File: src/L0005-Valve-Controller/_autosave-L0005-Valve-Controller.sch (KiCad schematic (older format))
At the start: 50 parts, among them J1 Jumper_NO, J2 Jumper_NO, P1 3220-20-0200-00, P10 353620650, P11 353620650, P12 353620650, P13 353620650, P14 647676-3, P15 647676-3, P2 140-504-415-000, P9 647676-2, U1 LPC54113J256BD64QL, U2 LMS8117AMP-3.3_NOPB, U3 MAX3370EXK+T, U4 MAX3370EXK+T

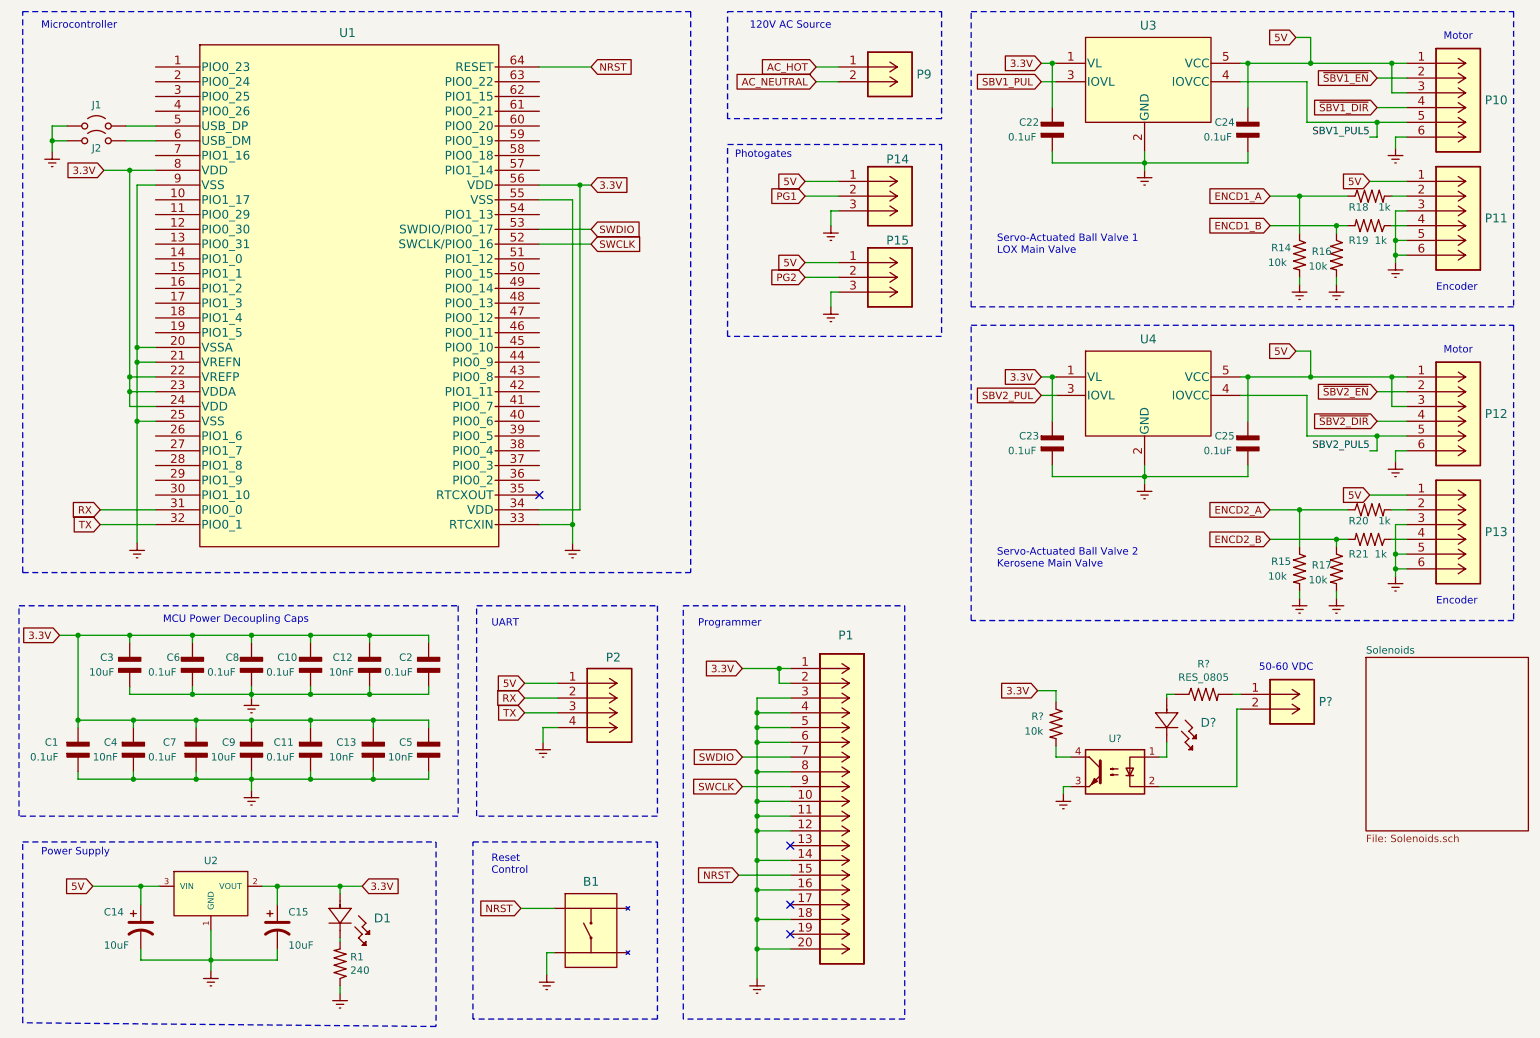
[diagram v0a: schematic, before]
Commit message: Added Red LED to lib files
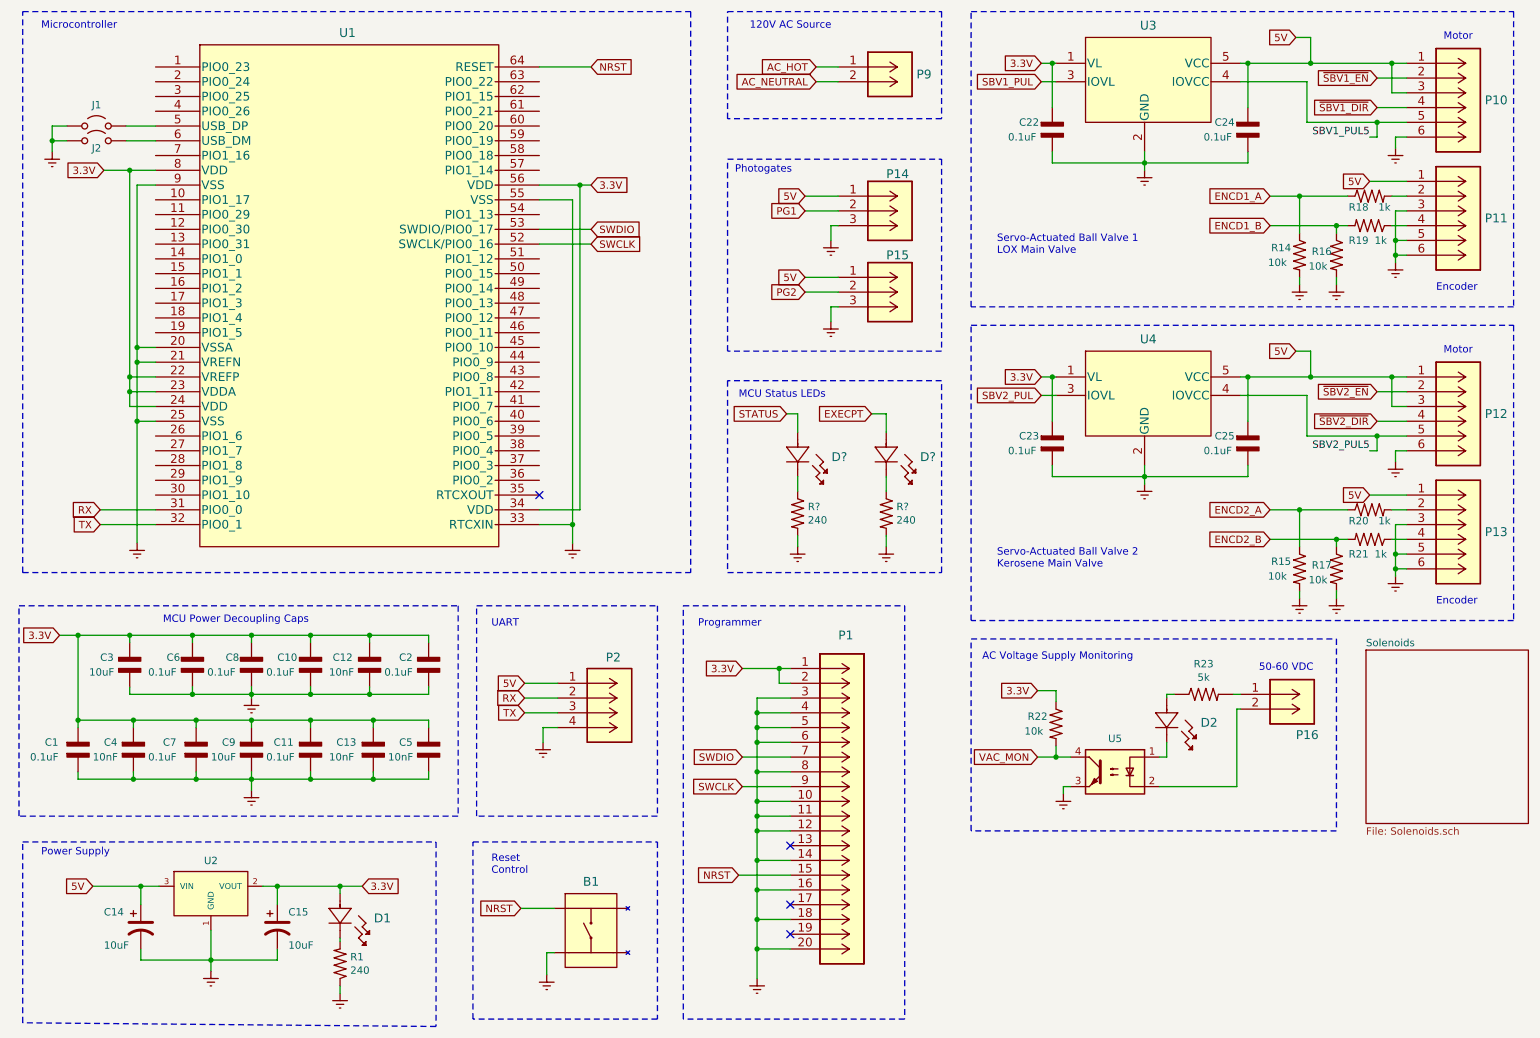
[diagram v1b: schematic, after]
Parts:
- added D?: LED_AMBER, symbol L0005-Valve-Controller:LED_AMBER
- added D?: LED_RED, symbol L0005-Valve-Controller:LED_RED
- added R? (x2): 240, symbol L0005-Valve-Controller:RES_0603
- R23: renamed from R?; value RES_0805 -> 5k
- gave numbers to parts that had none: 4
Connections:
- net Earth: now also R?.2, R?.2
- net VAC_MON: now reaches R22.2, U5.4
- new net: D?.1, R?.1 (x2)
- new net EXECPT: D?.2
- new net STATUS: D?.2
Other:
- note added: "AC Voltage Supply Monitoring"
- note added: "MCU Status LEDs"
- moved on the sheet: P14, P15
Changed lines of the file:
@@
 Microcontroller
 $Sheet
-S 9900 5125 1100 1175
+S 9900 5075 1100 1175
 U 624AA92C
 F0 "Solenoids" 50
@@
 L L0005-Valve-Controller:647676-3 P14
 U 1 1 62BF4641
-P 6325 1900
-F 0 "P14" H 6650 2050 60  0000 L CNN
-F 1 "647676-3" H 6675 1450 60  0001 C CNN
-F 2 "CONN_2043-1X04G00DAU_OUP" H 6675 1350 60  0001 C CNN
-F 3 "" H 6325 1900 60  0001 C CNN
-	1    6325 1900
-	1    0    0    -1
-$EndComp
-Text GLabel 6100 1900 0    50   Input ~ 0
+P 6325 2000
+F 0 "P14" H 6650 2150 60  0000 L CNN
+F 1 "647676-3" H 6675 1550 60  0001 C CNN
+F 2 "CONN_2043-1X04G00DAU_OUP" H 6675 1450 60  0001 C CNN
+F 3 "" H 6325 2000 60  0001 C CNN
+	1    6325 2000
+	1    0    0    -1
+$EndComp
+Text GLabel 6100 2000 0    50   Input ~ 0
 5V
 Wire Wire Line
-	6100 1900 6325 1900
+	6100 2000 6325 2000
 $Comp
 L L0005-Valve-Controller:Earth #PWR027
 U 1 1 62C26EB7
-P 6275 2200
-F 0 "#PWR027" H 6275 1950 50  0001 C CNN
-F 1 "Earth" H 6275 2050 50  0001 C CNN
-F 2 "" H 6275 2200 50  0001 C CNN
-F 3 "" H 6275 2200 50  0001 C CNN
-	1    6275 2200
-	1    0    0    -1
-$EndComp
-Wire Wire Line
-	6275 2200 6275 2100
-Wire Wire Line
-	6275 2100 6325 2100
-Text GLabel 6100 2000 0    50   Input ~ 0
+P 6275 2300
+F 0 "#PWR027" H 6275 2050 50  0001 C CNN
+F 1 "Earth" H 6275 2150 50  0001 C CNN
+F 2 "" H 6275 2300 50  0001 C CNN
+F 3 "" H 6275 2300 50  0001 C CNN
+	1    6275 2300
+	1    0    0    -1
+$EndComp
+Wire Wire Line
+	6275 2300 6275 2200
+Wire Wire Line
+	6275 2200 6325 2200
+Text GLabel 6100 2100 0    50   Input ~ 0
 PG1
 Wire Wire Line
-	6100 2000 6325 2000
+	6100 2100 6325 2100
 $Comp
 L L0005-Valve-Controller:647676-3 P15
 U 1 1 62C48E5C
-P 6325 2450
-F 0 "P15" H 6650 2600 60  0000 L CNN
-F 1 "647676-3" H 6675 2000 60  0001 C CNN
-F 2 "CONN_2043-1X04G00DAU_OUP" H 6675 1900 60  0001 C CNN
-F 3 "" H 6325 2450 60  0001 C CNN
-	1    6325 2450
-	1    0    0    -1
-$EndComp
-Text GLabel 6100 2450 0    50   Input ~ 0
+P 6325 2550
+F 0 "P15" H 6650 2700 60  0000 L CNN
+F 1 "647676-3" H 6675 2100 60  0001 C CNN
+F 2 "CONN_2043-1X04G00DAU_OUP" H 6675 2000 60  0001 C CNN
+F 3 "" H 6325 2550 60  0001 C CNN
+	1    6325 2550
+	1    0    0    -1
+$EndComp
+Text GLabel 6100 2550 0    50   Input ~ 0
 5V
 Wire Wire Line
-	6100 2450 6325 2450
+	6100 2550 6325 2550
 $Comp
 L L0005-Valve-Controller:Earth #PWR028
 U 1 1 62C48E64
-P 6275 2750
-F 0 "#PWR028" H 6275 2500 50  0001 C CNN
-F 1 "Earth" H 6275 2600 50  0001 C CNN
-F 2 "" H 6275 2750 50  0001 C CNN
-F 3 "" H 6275 2750 50  0001 C CNN
-	1    6275 2750
-	1    0    0    -1
-$EndComp
-Wire Wire Line
-	6275 2750 6275 2650
-Wire Wire Line
-	6275 2650 6325 2650
-Text GLabel 6100 2550 0    50   Input ~ 0
+P 6275 2850
+F 0 "#PWR028" H 6275 2600 50  0001 C CNN
+F 1 "Earth" H 6275 2700 50  0001 C CNN
+F 2 "" H 6275 2850 50  0001 C CNN
+F 3 "" H 6275 2850 50  0001 C CNN
+	1    6275 2850
+	1    0    0    -1
+$EndComp
+Wire Wire Line
+	6275 2850 6275 2750
+Wire Wire Line
+	6275 2750 6325 2750
+Text GLabel 6100 2650 0    50   Input ~ 0
 PG2
 Wire Wire Line
-	6100 2550 6325 2550
-Wire Notes Line
-	5575 1650 7025 1650
-Wire Notes Line
-	7025 1650 7025 2950
-Wire Notes Line
-	7025 2950 5575 2950
-Wire Notes Line
-	5575 2950 5575 1650
-Text Notes 5625 1750 0    50   ~ 0
+	6100 2650 6325 2650
+Wire Notes Line
+	5575 1750 7025 1750
+Wire Notes Line
+	7025 1750 7025 3050
+Wire Notes Line
+	7025 3050 5575 3050
+Wire Notes Line
+	5575 3050 5575 1750
+Text Notes 5625 1850 0    50   ~ 0
 Photogates
 $Comp
-L L0005-Valve-Controller:647676-2 P?
+L L0005-Valve-Controller:647676-2 P16
 U 1 1 61CE039C
 P 9050 5375
-F 0 "P?" H 9580 5325 60  0000 L CNN
+F 0 "P16" H 9425 5100 60  0000 L CNN
 F 1 "647676-2" H 9578 5272 60  0001 L CNN
 F 2 "CONN_2043-1X04G00DAU_OUP" H 9400 4825 60  0001 C CNN
@@
 	9025 5475 9050 5475
 $Comp
-L Engine-Controller:RES_0805 R?
+L Engine-Controller:RES_0805 R23
 U 1 1 61D6B512
 P 8800 5375
-F 0 "R?" H 8800 5581 50  0000 C CNN
-F 1 "RES_0805" H 8800 5490 50  0000 C CNN
+F 0 "R23" H 8800 5581 50  0000 C CNN
+F 1 "5k" H 8800 5490 50  0000 C CNN
 F 2 "" H 8850 4875 50  0001 L BNN
 F 3 "" H 8800 5375 50  0001 L BNN
@@
 $EndComp
 $Comp
-L L0005-Valve-Controller:Optocoupler U?
+L L0005-Valve-Controller:Optocoupler U5
 U 1 1 61D204C1
 P 8200 5900
-F 0 "U?" H 8200 6125 50  0000 C CNN
+F 0 "U5" H 8200 6125 50  0000 C CNN
 F 1 "Optocoupler" H 8200 6134 50  0001 C CNN
 F 2 "Package_DIP:DIP-4_W7.62mm" H 8000 5700 50  0001 L CIN
@@
 	8550 5800 8550 5700
 $Comp
-L L0005-Valve-Controller:LED_GREEN D?
+L L0005-Valve-Controller:LED_GREEN D2
 U 1 1 61D6FA18
 P 8550 5600
-F 0 "D?" H 8779 5633 60  0000 L CNN
+F 0 "D2" H 8779 5633 60  0000 L CNN
 F 1 "LED_GREEN" H 9000 5200 60  0001 C CNN
 F 2 "" H 8750 5240 60  0001 C CNN
@@
 	8500 6000 9025 6000
 $Comp
-L L0005-Valve-Controller:Earth #PWR?
+L L0005-Valve-Controller:Earth #PWR029
 U 1 1 61EE6B24
 P 7850 6050
-F 0 "#PWR?" H 7850 5800 50  0001 C CNN
+F 0 "#PWR029" H 7850 5800 50  0001 C CNN
 F 1 "Earth" H 7850 5900 50  0001 C CNN
 F 2 "" H 7850 6050 50  0001 C CNN
@@
 	7850 6000 7900 6000
 $Comp
-L L0005-Valve-Controller:RES_0603 R?
+L L0005-Valve-Controller:RES_0603 R22
 U 1 1 61EFDDA1
 P 7800 5575
-F 0 "R?" V 7750 5450 50  0000 C CNN
+F 0 "R22" V 7750 5450 50  0000 C CNN
 F 1 "10k" V 7850 5425 50  0000 C CNN
 F 2 "" H 7850 5075 50  0001 L BNN
@@
 Wire Wire Line
 	7800 5350 7800 5425
+Text GLabel 7675 5800 0    50   Input ~ 0
+VAC_MON
+Wire Wire Line
+	7675 5800 7800 5800
+Connection ~ 7800 5800
+Wire Notes Line
+	7225 5000 9700 5000
+Wire Notes Line
+	9700 5000 9700 6300
+Wire Notes Line
+	9700 6300 7225 6300
+Wire Notes Line
+	7225 6300 7225 5000
+Text Notes 7300 5150 0    50   ~ 0
+AC Voltage Supply Monitoring
+Text GLabel 5975 3475 0    50   Input ~ 0
+STATUS
+$Comp
+L L0005-Valve-Controller:LED_AMBER D?
+U 1 1 6201348C
+P 6050 3800
+F 0 "D?" H 6279 3833 60  0000 L CNN
+F 1 "LED_AMBER" H 6500 3400 60  0001 C CNN
+F 2 "" H 6250 3440 60  0001 C CNN
+F 3 "" V 6050 4050 60  0001 C CNN
+	1    6050 3800
+	1    0    0    -1
+$EndComp
+$Comp
+L L0005-Valve-Controller:RES_0603 R?
+U 1 1 6201850D
+P 6050 4150
+F 0 "R?" V 6004 4219 50  0000 L CNN
+F 1 "240" V 6095 4219 50  0000 L CNN
+F 2 "" H 6100 3650 50  0001 L BNN
+F 3 "" H 6050 4150 50  0001 L BNN
+	1    6050 4150
+	0    1    1    0
+$EndComp
+Wire Wire Line
+	5975 3475 6050 3475
+Wire Wire Line
+	6050 3475 6050 3600
+Wire Wire Line
+	6050 3900 6050 4000
+$Comp
+L L0005-Valve-Controller:Earth #PWR?
+U 1 1 620445E3
+P 6050 4375
+F 0 "#PWR?" H 6050 4125 50  0001 C CNN
+F 1 "Earth" H 6050 4225 50  0001 C CNN
+F 2 "" H 6050 4375 50  0001 C CNN
+F 3 "" H 6050 4375 50  0001 C CNN
+	1    6050 4375
+	1    0    0    -1
+$EndComp
+Wire Wire Line
+	6050 4375 6050 4300
+Text GLabel 6550 3475 0    50   Input ~ 0
+EXECPT
+Wire Wire Line
+	6550 3475 6650 3475
+Wire Wire Line
+	6650 3475 6650 3600
+$Comp
+L L0005-Valve-Controller:RES_0603 R?
+U 1 1 6207A00F
+P 6650 4150
+F 0 "R?" V 6604 4219 50  0000 L CNN
+F 1 "240" V 6695 4219 50  0000 L CNN
+F 2 "" H 6700 3650 50  0001 L BNN
+F 3 "" H 6650 4150 50  0001 L BNN
+	1    6650 4150
+	0    1    1    0
+$EndComp
+Wire Wire Line
+	6650 4000 6650 3900
+$Comp
+L L0005-Valve-Controller:Earth #PWR?
+U 1 1 6208D93F
+P 6650 4375
+F 0 "#PWR?" H 6650 4125 50  0001 C CNN
+F 1 "Earth" H 6650 4225 50  0001 C CNN
+F 2 "" H 6650 4375 50  0001 C CNN
+F 3 "" H 6650 4375 50  0001 C CNN
+	1    6650 4375
+	1    0    0    -1
+$EndComp
+Wire Wire Line
+	6650 4375 6650 4300
+$Comp
+L L0005-Valve-Controller:LED_RED D?
+U 1 1 620A6A1F
+P 6650 3800
+F 0 "D?" H 6879 3833 60  0000 L CNN
+F 1 "LED_RED" H 7100 3400 60  0001 C CNN
+F 2 "" H 6850 3440 60  0001 C CNN
+F 3 "" V 6650 4050 60  0001 C CNN
+	1    6650 3800
+	1    0    0    -1
+$EndComp
+Wire Notes Line
+	5575 4550 7025 4550
+Wire Notes Line
+	7025 4550 7025 3250
+Wire Notes Line
+	7025 3250 5575 3250
+Wire Notes Line
+	5575 3250 5575 4550
+Text Notes 5650 3375 0    50   ~ 0
+MCU Status LEDs
 $EndSCHEMATC
